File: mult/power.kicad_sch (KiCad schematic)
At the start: 5 parts, among them J5 Eurorack_Power

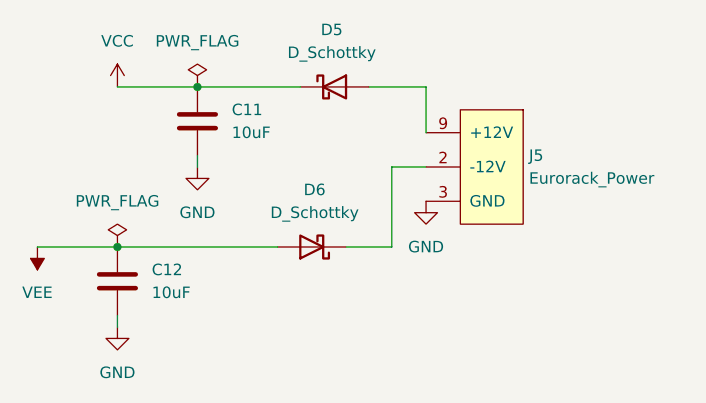
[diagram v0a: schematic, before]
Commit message: mult: Manually assign references, grouped by value
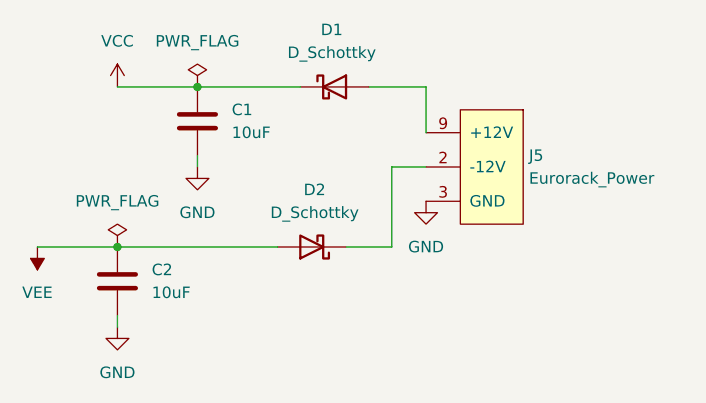
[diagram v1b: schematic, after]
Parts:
- renumbered C11 to C1, C12 to C2, D5 to D1, D6 to D2
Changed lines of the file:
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@@
   (symbol (lib_id "Device:C") (at 45.72 68.58 0) (unit 1)
     (in_bom yes) (on_board yes) (dnp no) (fields_autoplaced)
-    (property "Reference" "C12" (at 49.53 67.31 0)
+    (property "Reference" "C2" (at 49.53 67.31 0)
       (effects (font (size 1.27 1.27)) (justify left))
     )
@@
       (project "mult"
         (path "/0e98ec4b-b4c7-447c-abd7-a761177a7f67/8c1e2838-0bf6-4b12-a1e6-2b9765075731"
-          (reference "C12") (unit 1)
+          (reference "C2") (unit 1)
         )
       )
@@
   (symbol (lib_id "Device:D_Schottky") (at 69.85 46.99 0) (unit 1)
     (in_bom yes) (on_board yes) (dnp no) (fields_autoplaced)
-    (property "Reference" "D5" (at 69.5325 40.64 0)
+    (property "Reference" "D1" (at 69.5325 40.64 0)
       (effects (font (size 1.27 1.27)))
     )
@@
       (project "mult"
         (path "/0e98ec4b-b4c7-447c-abd7-a761177a7f67/8c1e2838-0bf6-4b12-a1e6-2b9765075731"
-          (reference "D5") (unit 1)
+          (reference "D1") (unit 1)
         )
       )
@@
   (symbol (lib_id "Device:C") (at 54.61 50.8 0) (unit 1)
     (in_bom yes) (on_board yes) (dnp no) (fields_autoplaced)
-    (property "Reference" "C11" (at 58.42 49.53 0)
+    (property "Reference" "C1" (at 58.42 49.53 0)
       (effects (font (size 1.27 1.27)) (justify left))
     )
@@
       (project "mult"
         (path "/0e98ec4b-b4c7-447c-abd7-a761177a7f67/8c1e2838-0bf6-4b12-a1e6-2b9765075731"
-          (reference "C11") (unit 1)
+          (reference "C1") (unit 1)
         )
       )
@@
   (symbol (lib_id "Device:D_Schottky") (at 67.31 64.77 180) (unit 1)
     (in_bom yes) (on_board yes) (dnp no) (fields_autoplaced)
-    (property "Reference" "D6" (at 67.6275 58.42 0)
+    (property "Reference" "D2" (at 67.6275 58.42 0)
       (effects (font (size 1.27 1.27)))
     )
@@
       (project "mult"
         (path "/0e98ec4b-b4c7-447c-abd7-a761177a7f67/8c1e2838-0bf6-4b12-a1e6-2b9765075731"
-          (reference "D6") (unit 1)
+          (reference "D2") (unit 1)
         )
       )
@@
         )
         (path "/0e98ec4b-b4c7-447c-abd7-a761177a7f67/8c1e2838-0bf6-4b12-a1e6-2b9765075731"
-          (reference "J5") (unit 1)
-        )
-      )
+          (reference "J1") (unit 1)
+        )
+      )

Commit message: mult: Assign footprints
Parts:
- C1, C2: footprint (none) -> Capacitor_SMD:C_0805_2012Metric
- D1, D2: footprint (none) -> Diode_SMD:D_SOD-123
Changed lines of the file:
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@@
       (effects (font (size 1.27 1.27)) (justify left))
     )
-    (property "Footprint" "" (at 46.6852 72.39 0)
+    (property "Footprint" "Capacitor_SMD:C_0805_2012Metric" (at 46.6852 72.39 0)
       (effects (font (size 1.27 1.27)) hide)
     )
@@
       (effects (font (size 1.27 1.27)))
     )
-    (property "Footprint" "" (at 69.85 46.99 0)
+    (property "Footprint" "Diode_SMD:D_SOD-123" (at 69.85 46.99 0)
       (effects (font (size 1.27 1.27)) hide)
     )
@@
       (effects (font (size 1.27 1.27)) (justify left))
     )
-    (property "Footprint" "" (at 55.5752 54.61 0)
+    (property "Footprint" "Capacitor_SMD:C_0805_2012Metric" (at 55.5752 54.61 0)
       (effects (font (size 1.27 1.27)) hide)
     )
@@
       (effects (font (size 1.27 1.27)))
     )
-    (property "Footprint" "" (at 67.31 64.77 0)
+    (property "Footprint" "Diode_SMD:D_SOD-123" (at 67.31 64.77 0)
       (effects (font (size 1.27 1.27)) hide)
     )

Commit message: mult: Misc partial progress
At least since last commit:

* New LEDs (no dual unit)
* Jack placement, share sleeve pin
* Board fit within 20x108mm
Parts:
- C1, C2: footprint Capacitor_SMD:C_0805_2012Metric -> Capacitor_SMD:C_0805_2012Metric_Pad1.18x1.45mm_HandSolder
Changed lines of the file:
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@@
       (effects (font (size 1.27 1.27)) (justify left))
     )
-    (property "Footprint" "Capacitor_SMD:C_0805_2012Metric" (at 46.6852 72.39 0)
+    (property "Footprint" "Capacitor_SMD:C_0805_2012Metric_Pad1.18x1.45mm_HandSolder" (at 46.6852 72.39 0)
       (effects (font (size 1.27 1.27)) hide)
     )
@@
       (effects (font (size 1.27 1.27)) (justify left))
     )
-    (property "Footprint" "Capacitor_SMD:C_0805_2012Metric" (at 55.5752 54.61 0)
+    (property "Footprint" "Capacitor_SMD:C_0805_2012Metric_Pad1.18x1.45mm_HandSolder" (at 55.5752 54.61 0)
       (effects (font (size 1.27 1.27)) hide)
     )

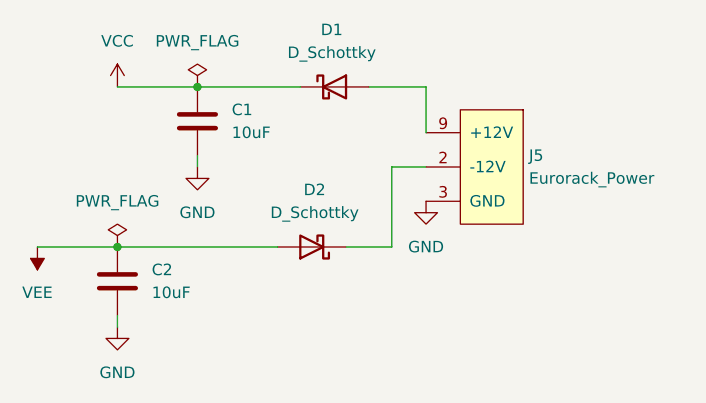
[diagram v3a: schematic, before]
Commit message: mult: Progress rerouting easier layout
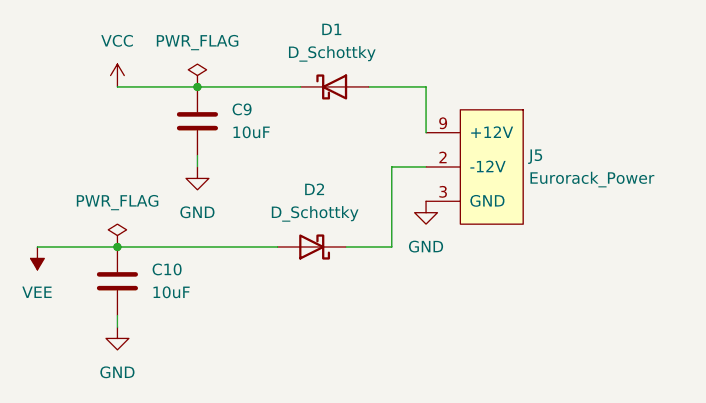
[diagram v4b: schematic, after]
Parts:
- renumbered C2 to C10, C1 to C9
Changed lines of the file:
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@@
   (symbol (lib_id "Device:C") (at 45.72 68.58 0) (unit 1)
     (in_bom yes) (on_board yes) (dnp no) (fields_autoplaced)
-    (property "Reference" "C2" (at 49.53 67.31 0)
+    (property "Reference" "C10" (at 49.53 67.31 0)
       (effects (font (size 1.27 1.27)) (justify left))
     )
@@
       (project "mult"
         (path "/0e98ec4b-b4c7-447c-abd7-a761177a7f67/8c1e2838-0bf6-4b12-a1e6-2b9765075731"
-          (reference "C2") (unit 1)
+          (reference "C10") (unit 1)
         )
       )
@@
         )
         (path "/0e98ec4b-b4c7-447c-abd7-a761177a7f67/8c1e2838-0bf6-4b12-a1e6-2b9765075731"
-          (reference "#PWR010") (unit 1)
+          (reference "#PWR038") (unit 1)
         )
       )
@@
   (symbol (lib_id "Device:C") (at 54.61 50.8 0) (unit 1)
     (in_bom yes) (on_board yes) (dnp no) (fields_autoplaced)
-    (property "Reference" "C1" (at 58.42 49.53 0)
+    (property "Reference" "C9" (at 58.42 49.53 0)
       (effects (font (size 1.27 1.27)) (justify left))
     )
@@
       (project "mult"
         (path "/0e98ec4b-b4c7-447c-abd7-a761177a7f67/8c1e2838-0bf6-4b12-a1e6-2b9765075731"
-          (reference "C1") (unit 1)
+          (reference "C9") (unit 1)
         )
       )
@@
         )
         (path "/0e98ec4b-b4c7-447c-abd7-a761177a7f67/8c1e2838-0bf6-4b12-a1e6-2b9765075731"
-          (reference "#PWR055") (unit 1)
+          (reference "#PWR041") (unit 1)
         )
       )
@@
         )
         (path "/0e98ec4b-b4c7-447c-abd7-a761177a7f67/8c1e2838-0bf6-4b12-a1e6-2b9765075731"
-          (reference "#PWR056") (unit 1)
+          (reference "#PWR040") (unit 1)
         )
       )
@@
         )
         (path "/0e98ec4b-b4c7-447c-abd7-a761177a7f67/8c1e2838-0bf6-4b12-a1e6-2b9765075731"
-          (reference "J1") (unit 1)
+          (reference "J17") (unit 1)
         )
       )
@@
   (symbol (lib_id "power:GND") (at 54.61 55.88 0) (unit 1)
     (in_bom yes) (on_board yes) (dnp no) (fields_autoplaced)
-    (property "Reference" "#PWR057" (at 54.61 62.23 0)
+    (property "Reference" "#PWR039" (at 54.61 62.23 0)
       (effects (font (size 1.27 1.27)) hide)
     )
@@
       (project "mult"
         (path "/0e98ec4b-b4c7-447c-abd7-a761177a7f67/8c1e2838-0bf6-4b12-a1e6-2b9765075731"
-          (reference "#PWR057") (unit 1)
+          (reference "#PWR039") (unit 1)
         )
       )
@@
   (symbol (lib_id "power:GND") (at 45.72 73.66 0) (unit 1)
     (in_bom yes) (on_board yes) (dnp no) (fields_autoplaced)
-    (property "Reference" "#PWR058" (at 45.72 80.01 0)
+    (property "Reference" "#PWR042" (at 45.72 80.01 0)
       (effects (font (size 1.27 1.27)) hide)
     )
@@
       (project "mult"
         (path "/0e98ec4b-b4c7-447c-abd7-a761177a7f67/8c1e2838-0bf6-4b12-a1e6-2b9765075731"
-          (reference "#PWR058") (unit 1)
-        )
-      )
+          (reference "#PWR042") (unit 1)
+        )
+      )

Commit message: mult: Reassign reference designators
This follows visual placement (left to right, top to bottom), except for
bulk capacitors which are enumerated left to right after bypass caps.
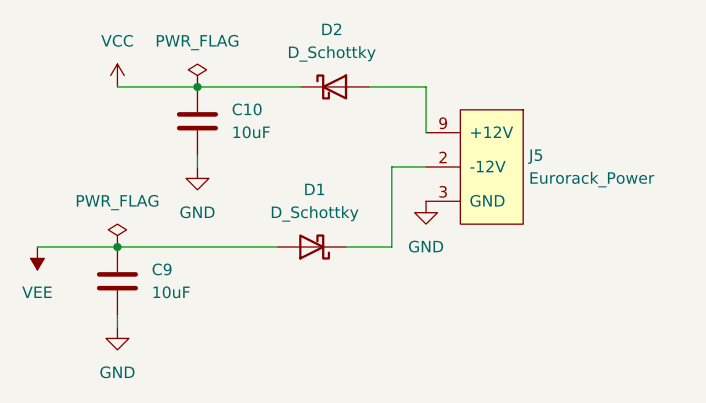
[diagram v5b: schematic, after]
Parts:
- renumbered C9 to C10, C10 to C9, D2 to D1, D1 to D2
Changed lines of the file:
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@@
   (symbol (lib_id "Device:C") (at 45.72 68.58 0) (unit 1)
     (in_bom yes) (on_board yes) (dnp no) (fields_autoplaced)
-    (property "Reference" "C10" (at 49.53 67.31 0)
+    (property "Reference" "C9" (at 49.53 67.31 0)
       (effects (font (size 1.27 1.27)) (justify left))
     )
@@
       (project "mult"
         (path "/0e98ec4b-b4c7-447c-abd7-a761177a7f67/8c1e2838-0bf6-4b12-a1e6-2b9765075731"
-          (reference "C10") (unit 1)
+          (reference "C9") (unit 1)
         )
       )
@@
   (symbol (lib_id "Device:D_Schottky") (at 69.85 46.99 0) (unit 1)
     (in_bom yes) (on_board yes) (dnp no) (fields_autoplaced)
-    (property "Reference" "D1" (at 69.5325 40.64 0)
+    (property "Reference" "D2" (at 69.5325 40.64 0)
       (effects (font (size 1.27 1.27)))
     )
@@
       (project "mult"
         (path "/0e98ec4b-b4c7-447c-abd7-a761177a7f67/8c1e2838-0bf6-4b12-a1e6-2b9765075731"
-          (reference "D1") (unit 1)
+          (reference "D2") (unit 1)
         )
       )
@@
   (symbol (lib_id "Device:C") (at 54.61 50.8 0) (unit 1)
     (in_bom yes) (on_board yes) (dnp no) (fields_autoplaced)
-    (property "Reference" "C9" (at 58.42 49.53 0)
+    (property "Reference" "C10" (at 58.42 49.53 0)
       (effects (font (size 1.27 1.27)) (justify left))
     )
@@
       (project "mult"
         (path "/0e98ec4b-b4c7-447c-abd7-a761177a7f67/8c1e2838-0bf6-4b12-a1e6-2b9765075731"
-          (reference "C9") (unit 1)
+          (reference "C10") (unit 1)
         )
       )
@@
   (symbol (lib_id "Device:D_Schottky") (at 67.31 64.77 180) (unit 1)
     (in_bom yes) (on_board yes) (dnp no) (fields_autoplaced)
-    (property "Reference" "D2" (at 67.6275 58.42 0)
+    (property "Reference" "D1" (at 67.6275 58.42 0)
       (effects (font (size 1.27 1.27)))
     )
@@
       (project "mult"
         (path "/0e98ec4b-b4c7-447c-abd7-a761177a7f67/8c1e2838-0bf6-4b12-a1e6-2b9765075731"
-          (reference "D2") (unit 1)
+          (reference "D1") (unit 1)
         )
       )
